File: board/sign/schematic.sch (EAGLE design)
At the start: 37 parts, among them IC1 STM32F207ZGT, IC3 LM3940, J1 DCJ0202, X2 22-23-2041

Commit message: Board REV A done
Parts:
- C24: device rcl:CPOL-USA -> rcl:CPOL-USE2-5
- JP2: device con-lstb:MA04-1 -> con-lstb:MA05-1
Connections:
- net DEBUG_TX: now also JP2.5
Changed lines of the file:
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@@
 <part name="IC3" library="LM3940" deviceset="LM3940" device=""/>
 <part name="C23" library="rcl" library_urn="urn:adsk.eagle:library:334" deviceset="C-EU" device="025-025X050" package3d_urn="urn:adsk.eagle:package:23629/2" value="0.47uF"/>
-<part name="C24" library="rcl" library_urn="urn:adsk.eagle:library:334" deviceset="CPOL-US" device="A" package3d_urn="urn:adsk.eagle:package:23418/2" value="33uF"/>
-<part name="JP2" library="con-lstb" library_urn="urn:adsk.eagle:library:162" deviceset="MA04-1" device="" package3d_urn="urn:adsk.eagle:package:8337/1"/>
+<part name="C24" library="rcl" library_urn="urn:adsk.eagle:library:334" deviceset="CPOL-US" device="E2-5" package3d_urn="urn:adsk.eagle:package:23346/2" value="33uF"/>
+<part name="JP2" library="con-lstb" library_urn="urn:adsk.eagle:library:162" deviceset="MA05-1" device="" package3d_urn="urn:adsk.eagle:package:8332/1"/>
 <part name="JP1" library="pinhead" library_urn="urn:adsk.eagle:library:325" deviceset="PINHD-2X8" device="" package3d_urn="urn:adsk.eagle:package:22481/2"/>
 <part name="GND18" library="supply1" library_urn="urn:adsk.eagle:library:371" deviceset="GND" device=""/>
@@
 <attribute name="VALUE" x="227.076" y="224.409" size="1.778" layer="96"/>
 </instance>
-<instance part="JP2" gate="1" x="307.34" y="101.6" smashed="yes" rot="R180">
+<instance part="JP2" gate="G$1" x="307.34" y="101.6" smashed="yes" rot="R180">
 <attribute name="VALUE" x="308.61" y="111.76" size="1.778" layer="96" rot="R180"/>
-<attribute name="NAME" x="308.61" y="95.758" size="1.778" layer="95" rot="R180"/>
+<attribute name="NAME" x="313.69" y="98.298" size="1.778" layer="95" rot="R180"/>
 </instance>
 <instance part="JP1" gate="A" x="299.72" y="76.2" smashed="yes">
@@
 <pinref part="GND19" gate="1" pin="GND"/>
 <wire x1="279.4" y1="91.44" x2="279.4" y2="99.06" width="0.1524" layer="91"/>
-<pinref part="JP2" gate="1" pin="4"/>
+<pinref part="JP2" gate="G$1" pin="4"/>
 <wire x1="279.4" y1="99.06" x2="299.72" y2="99.06" width="0.1524" layer="91"/>
 </segment>
@@
 </segment>
 <segment>
-<pinref part="JP2" gate="1" pin="1"/>
+<pinref part="JP2" gate="G$1" pin="1"/>
 <wire x1="299.72" y1="106.68" x2="284.48" y2="106.68" width="0.1524" layer="91"/>
 <pinref part="+3V9" gate="G$1" pin="+3V3"/>
@@
 <junction x="83.82" y="33.02"/>
 </segment>
+<segment>
+<pinref part="JP2" gate="G$1" pin="5"/>
+<wire x1="299.72" y1="96.52" x2="281.94" y2="96.52" width="0.1524" layer="91"/>
+<label x="281.94" y="96.52" size="1.778" layer="95"/>
+</segment>
 </net>
 <net name="N$4" class="0">
@@
 </segment>
 <segment>
-<pinref part="JP2" gate="1" pin="2"/>
+<pinref part="JP2" gate="G$1" pin="2"/>
 <wire x1="299.72" y1="104.14" x2="279.4" y2="104.14" width="0.1524" layer="91"/>
 <label x="279.4" y="104.14" size="1.778" layer="95"/>
@@
 </segment>
 <segment>
-<pinref part="JP2" gate="1" pin="3"/>
+<pinref part="JP2" gate="G$1" pin="3"/>
 <wire x1="299.72" y1="101.6" x2="279.4" y2="101.6" width="0.1524" layer="91"/>
 <label x="279.4" y="101.6" size="1.778" layer="95"/>
@@
 </sheet>
 </sheets>
+<errors>
+</errors>
 </schematic>
 </drawing>

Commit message: Fix SD
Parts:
- removed U$1: MICROSD, micro-sd:MICROSD
- added J2: 2908-05WB-MG, 2908-05WB-MG:2908-05WB-MG
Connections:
- net +3V3: now also J2.VDD; no longer U$1.VDD
- net GND: now also J2.VSS; no longer U$1.GND, U$1.SHIELD@1, U$1.SHIELD@2, U$1.SHIELD@3, U$1.SHIELD@4
- net MISO: now also J2.DAT0; no longer U$1.DAT0/DO
- net MOSI: now also J2.CMD; no longer U$1.CMD/DI
- net SCLK: now also J2.CLK; no longer U$1.CLK/SCLK
- net SDCS: now also J2.DAT3/CD; no longer U$1.CD/DAT3/CS
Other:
- moved on the sheet: C21
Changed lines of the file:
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@@
 <part name="R2" library="rcl" library_urn="urn:adsk.eagle:library:334" deviceset="R-US_" device="0204/7" package3d_urn="urn:adsk.eagle:package:23498/1" value="12k"/>
 <part name="GND11" library="supply1" library_urn="urn:adsk.eagle:library:371" deviceset="GND" device=""/>
-<part name="U$1" library="micro-sd" deviceset="MICROSD" device=""/>
 <part name="+3V5" library="supply1" library_urn="urn:adsk.eagle:library:371" deviceset="+3V3" device=""/>
-<part name="GND12" library="supply1" library_urn="urn:adsk.eagle:library:371" deviceset="GND" device=""/>
 <part name="C21" library="rcl" library_urn="urn:adsk.eagle:library:334" deviceset="C-EU" device="025-025X050" package3d_urn="urn:adsk.eagle:package:23629/2" value="100nF"/>
 <part name="GND13" library="supply1" library_urn="urn:adsk.eagle:library:371" deviceset="GND" device=""/>
@@
 <part name="+3V2" library="supply1" library_urn="urn:adsk.eagle:library:371" deviceset="+3V3" device=""/>
 <part name="+3V11" library="supply1" library_urn="urn:adsk.eagle:library:371" deviceset="+3V3" device=""/>
+<part name="J2" library="2908-05WB-MG" deviceset="2908-05WB-MG" device=""/>
+<part name="GND20" library="supply1" library_urn="urn:adsk.eagle:library:371" deviceset="GND" device=""/>
 </parts>
 <sheets>
@@
 <attribute name="VALUE" x="86.36" y="15.24" size="1.778" layer="96"/>
 </instance>
-<instance part="U$1" gate="G$1" x="236.22" y="88.9" smashed="yes"/>
-<instance part="+3V5" gate="G$1" x="208.28" y="114.3" smashed="yes">
-<attribute name="VALUE" x="205.74" y="109.22" size="1.778" layer="96" rot="R90"/>
-</instance>
-<instance part="GND12" gate="1" x="208.28" y="55.88" smashed="yes">
-<attribute name="VALUE" x="205.74" y="53.34" size="1.778" layer="96"/>
-</instance>
-<instance part="C21" gate="G$1" x="205.74" y="106.68" smashed="yes" rot="R270">
-<attribute name="NAME" x="206.121" y="105.156" size="1.778" layer="95" rot="R270"/>
-<attribute name="VALUE" x="201.041" y="105.156" size="1.778" layer="96" rot="R270"/>
-</instance>
-<instance part="GND13" gate="1" x="198.12" y="106.68" smashed="yes" rot="R270">
-<attribute name="VALUE" x="195.58" y="109.22" size="1.778" layer="96" rot="R270"/>
+<instance part="+3V5" gate="G$1" x="266.7" y="109.22" smashed="yes" rot="R270">
+<attribute name="VALUE" x="261.62" y="111.76" size="1.778" layer="96"/>
+</instance>
+<instance part="C21" gate="G$1" x="259.08" y="111.76" smashed="yes" rot="R180">
+<attribute name="NAME" x="257.556" y="111.379" size="1.778" layer="95" rot="R180"/>
+<attribute name="VALUE" x="257.556" y="116.459" size="1.778" layer="96" rot="R180"/>
+</instance>
+<instance part="GND13" gate="1" x="259.08" y="119.38" smashed="yes" rot="R180">
+<attribute name="VALUE" x="261.62" y="121.92" size="1.778" layer="96" rot="R180"/>
 </instance>
 <instance part="X2" gate="-1" x="162.56" y="127" smashed="yes">
@@
 <instance part="+3V11" gate="G$1" x="289.56" y="215.9" smashed="yes">
 <attribute name="VALUE" x="287.02" y="210.82" size="1.778" layer="96" rot="R90"/>
+</instance>
+<instance part="J2" gate="G$1" x="238.76" y="93.98" smashed="yes">
+<attribute name="NAME" x="228.5841" y="104.1559" size="1.271990625" layer="95"/>
+<attribute name="VALUE" x="228.5925" y="81.2706" size="1.270940625" layer="96"/>
+</instance>
+<instance part="GND20" gate="1" x="259.08" y="78.74" smashed="yes">
+<attribute name="VALUE" x="256.54" y="76.2" size="1.778" layer="96"/>
 </instance>
 </instances>
@@
 </segment>
 <segment>
-<pinref part="GND12" gate="1" pin="GND"/>
-<pinref part="U$1" gate="G$1" pin="SHIELD@4"/>
-<wire x1="208.28" y1="58.42" x2="208.28" y2="68.58" width="0.1524" layer="91"/>
-<wire x1="208.28" y1="68.58" x2="215.9" y2="68.58" width="0.1524" layer="91"/>
-<pinref part="U$1" gate="G$1" pin="SHIELD@2"/>
-<wire x1="215.9" y1="73.66" x2="208.28" y2="73.66" width="0.1524" layer="91"/>
-<wire x1="208.28" y1="73.66" x2="208.28" y2="71.12" width="0.1524" layer="91"/>
-<junction x="208.28" y="68.58"/>
-<pinref part="U$1" gate="G$1" pin="SHIELD@3"/>
-<wire x1="208.28" y1="71.12" x2="208.28" y2="68.58" width="0.1524" layer="91"/>
-<wire x1="208.28" y1="71.12" x2="215.9" y2="71.12" width="0.1524" layer="91"/>
-<junction x="208.28" y="71.12"/>
-<pinref part="U$1" gate="G$1" pin="SHIELD@1"/>
-<wire x1="215.9" y1="76.2" x2="208.28" y2="76.2" width="0.1524" layer="91"/>
-<wire x1="208.28" y1="76.2" x2="208.28" y2="73.66" width="0.1524" layer="91"/>
-<junction x="208.28" y="73.66"/>
-<pinref part="U$1" gate="G$1" pin="GND"/>
-<wire x1="215.9" y1="78.74" x2="208.28" y2="78.74" width="0.1524" layer="91"/>
-<wire x1="208.28" y1="78.74" x2="208.28" y2="76.2" width="0.1524" layer="91"/>
-<junction x="208.28" y="76.2"/>
-</segment>
-<segment>
 <pinref part="C21" gate="G$1" pin="2"/>
 <pinref part="GND13" gate="1" pin="GND"/>
@@
 <pinref part="GND2" gate="1" pin="GND"/>
 <junction x="20.32" y="119.38"/>
+</segment>
+<segment>
+<pinref part="GND20" gate="1" pin="GND"/>
+<wire x1="259.08" y1="81.28" x2="259.08" y2="86.36" width="0.1524" layer="91"/>
+<pinref part="J2" gate="G$1" pin="VSS"/>
+<wire x1="259.08" y1="86.36" x2="254" y2="86.36" width="0.1524" layer="91"/>
 </segment>
 </net>
@@
 <segment>
 <pinref part="+3V5" gate="G$1" pin="+3V3"/>
-<pinref part="U$1" gate="G$1" pin="VDD"/>
-<wire x1="208.28" y1="111.76" x2="208.28" y2="106.68" width="0.1524" layer="91"/>
-<wire x1="208.28" y1="106.68" x2="215.9" y2="106.68" width="0.1524" layer="91"/>
+<wire x1="264.16" y1="109.22" x2="259.08" y2="109.22" width="0.1524" layer="91"/>
+<wire x1="259.08" y1="109.22" x2="259.08" y2="101.6" width="0.1524" layer="91"/>
 <pinref part="C21" gate="G$1" pin="1"/>
-<junction x="208.28" y="106.68"/>
+<junction x="259.08" y="109.22"/>
+<pinref part="J2" gate="G$1" pin="VDD"/>
+<wire x1="259.08" y1="101.6" x2="254" y2="101.6" width="0.1524" layer="91"/>
 </segment>
 <segment>
@@
 <net name="SCLK" class="0">
 <segment>
-<pinref part="U$1" gate="G$1" pin="CLK/SCLK"/>
-<wire x1="215.9" y1="99.06" x2="187.96" y2="99.06" width="0.1524" layer="91"/>
-<label x="187.96" y="99.06" size="1.778" layer="95"/>
-</segment>
-<segment>
 <pinref part="IC2" gate="G$1" pin="GPIO14"/>
 <wire x1="27.94" y1="35.56" x2="17.78" y2="35.56" width="0.1524" layer="91"/>
 <label x="17.78" y="35.56" size="1.778" layer="95"/>
 </segment>
+<segment>
+<pinref part="J2" gate="G$1" pin="CLK"/>
+<wire x1="223.52" y1="86.36" x2="208.28" y2="86.36" width="0.1524" layer="91"/>
+<label x="208.28" y="86.36" size="1.778" layer="95"/>
+</segment>
 </net>
 <net name="MOSI" class="0">
-<segment>
-<pinref part="U$1" gate="G$1" pin="CMD/DI"/>
-<wire x1="215.9" y1="101.6" x2="187.96" y2="101.6" width="0.1524" layer="91"/>
-<label x="187.96" y="101.6" size="1.778" layer="95"/>
-</segment>
 <segment>
 <pinref part="IC2" gate="G$1" pin="GPIO4"/>
@@
 <label x="68.58" y="48.26" size="1.778" layer="95" rot="R90"/>
 </segment>
+<segment>
+<pinref part="J2" gate="G$1" pin="CMD"/>
+<wire x1="223.52" y1="91.44" x2="208.28" y2="91.44" width="0.1524" layer="91"/>
+<label x="208.28" y="91.44" size="1.778" layer="95"/>
+</segment>
 </net>
 <net name="MISO" class="0">
-<segment>
-<pinref part="U$1" gate="G$1" pin="DAT0/DO"/>
-<wire x1="215.9" y1="96.52" x2="187.96" y2="96.52" width="0.1524" layer="91"/>
-<label x="187.96" y="96.52" size="1.778" layer="95"/>
-</segment>
 <segment>
 <pinref part="IC2" gate="G$1" pin="GPIO12"/>
@@
 <label x="10.16" y="33.02" size="1.778" layer="95"/>
 </segment>
+<segment>
+<pinref part="J2" gate="G$1" pin="DAT0"/>
+<wire x1="223.52" y1="101.6" x2="208.28" y2="101.6" width="0.1524" layer="91"/>
+<label x="208.28" y="101.6" size="1.778" layer="95"/>
+</segment>
 </net>
 <net name="SDCS" class="0">
-<segment>
-<pinref part="U$1" gate="G$1" pin="CD/DAT3/CS"/>
-<wire x1="215.9" y1="88.9" x2="187.96" y2="88.9" width="0.1524" layer="91"/>
-<label x="187.96" y="88.9" size="1.778" layer="95"/>
-</segment>
 <segment>
 <pinref part="IC2" gate="G$1" pin="GPIO5"/>
@@
 <label x="66.04" y="48.26" size="1.778" layer="95" rot="R90"/>
 </segment>
-</net>
+<segment>
+<pinref part="J2" gate="G$1" pin="DAT3/CD"/>
+<wire x1="223.52" y1="93.98" x2="208.28" y2="93.98" width="0.1524" layer="91"/>
+<label x="208.28" y="93.98" size="1.778" layer="95"/>
+</segment>
+</net>

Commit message: Final board
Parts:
- removed J2: 2908-05WB-MG, 2908-05WB-MG:2908-05WB-MG
- added J3: DM3AT-SF-PEJM5, connector:DM3AT-SF-PEJM5
- added R5: 470, rcl:R-US_0204/7
- added S2: (no value), switch-omron:10-XX
- C19: device rcl:C-EU025-025X050 -> rcl:CPOL-USE2.5-6
- C2, C23: device rcl:C-EU025-025X050 -> rcl:C-EU050-024X044
- C4, C5: device rcl:C-EU025-025X050 -> rcl:CPOL-USE1.8-4
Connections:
- removed net N$4: IC2.GPIO0, R3.2
- new net FLASH: IC2.GPIO0, R3.2, R5.2
- new net N$1: R5.1, S2.S, S2.S1
- net +3V3: now also C19.+, J3.VCC; no longer C19.1, J2.VDD
- net GND: now also C19.-, C4.-, C5.-, J3.GND, S2.P, S2.P1; no longer C19.2, C4.1, C5.1, J2.VSS
- net MISO: now also J3.DATA0/MISO; no longer J2.DAT0
- net MOSI: now also J3.CMD/MOSI; no longer J2.CMD
- net N$2: now also C5.+; no longer C5.2
- net N$3: now also C4.+; no longer C4.2
- net SCLK: now also J3.CLK; no longer J2.CLK
- net SDCS: now also J3.DATA3-CD/CS_N; no longer J2.DAT3/CD
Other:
- moved on the sheet: C21

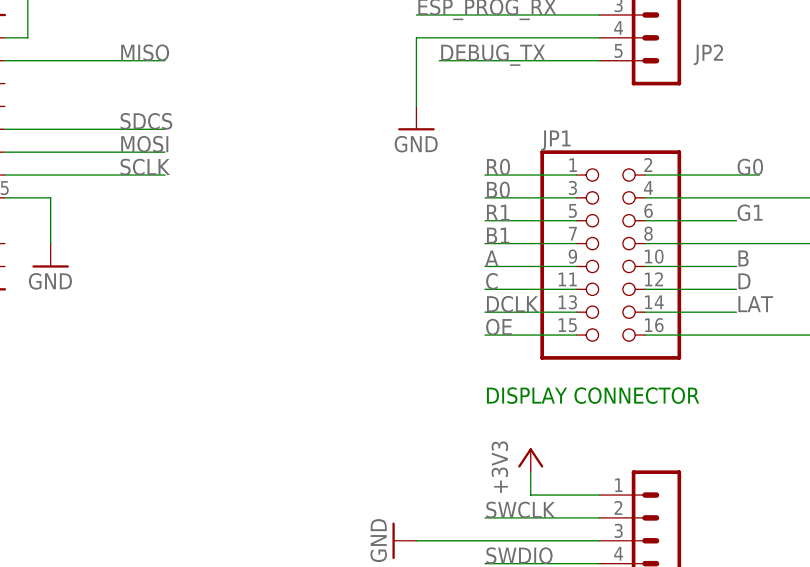
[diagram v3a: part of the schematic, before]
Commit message: Add noise-cleanup cap
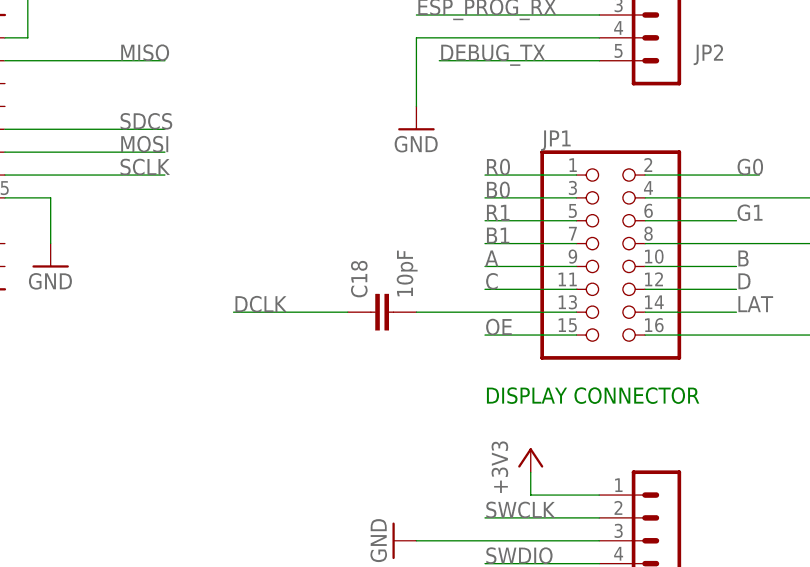
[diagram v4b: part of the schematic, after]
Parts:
- added C18: 10pF, rcl:C-EU050-024X044
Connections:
- new net N$4: C18.2, JP1.13
- net DCLK: now also C18.1; no longer JP1.13
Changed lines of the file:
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@@
 <part name="GND4" library="supply1" library_urn="urn:adsk.eagle:library:371" deviceset="GND" device=""/>
 <part name="J3" library="connector" deviceset="DM3AT-SF-PEJM5" device=""/>
+<part name="C18" library="rcl" library_urn="urn:adsk.eagle:library:334" deviceset="C-EU" device="050-024X044" package3d_urn="urn:adsk.eagle:package:23643/1" value="10pF"/>
 </parts>
 <sheets>
@@
 <attribute name="VALUE" x="205.74" y="68.58" size="1.27" layer="96"/>
 </instance>
+<instance part="C18" gate="G$1" x="274.32" y="68.58" smashed="yes" rot="R90">
+<attribute name="NAME" x="273.939" y="70.104" size="1.778" layer="95" rot="R90"/>
+<attribute name="VALUE" x="279.019" y="70.104" size="1.778" layer="96" rot="R90"/>
+</instance>
 </instances>
 <busses>
@@
 </segment>
 <segment>
-<pinref part="JP1" gate="A" pin="13"/>
-<wire x1="297.18" y1="68.58" x2="287.02" y2="68.58" width="0.1524" layer="91"/>
-<label x="287.02" y="68.58" size="1.778" layer="95"/>
+<pinref part="C18" gate="G$1" pin="1"/>
+<wire x1="271.78" y1="68.58" x2="259.08" y2="68.58" width="0.1524" layer="91"/>
+<label x="259.08" y="68.58" size="1.778" layer="95"/>
 </segment>
 </net>
@@
 </segment>
 </net>
+<net name="N$4" class="0">
+<segment>
+<pinref part="JP1" gate="A" pin="13"/>
+<pinref part="C18" gate="G$1" pin="2"/>
+<wire x1="297.18" y1="68.58" x2="279.4" y2="68.58" width="0.1524" layer="91"/>
+</segment>
+</net>

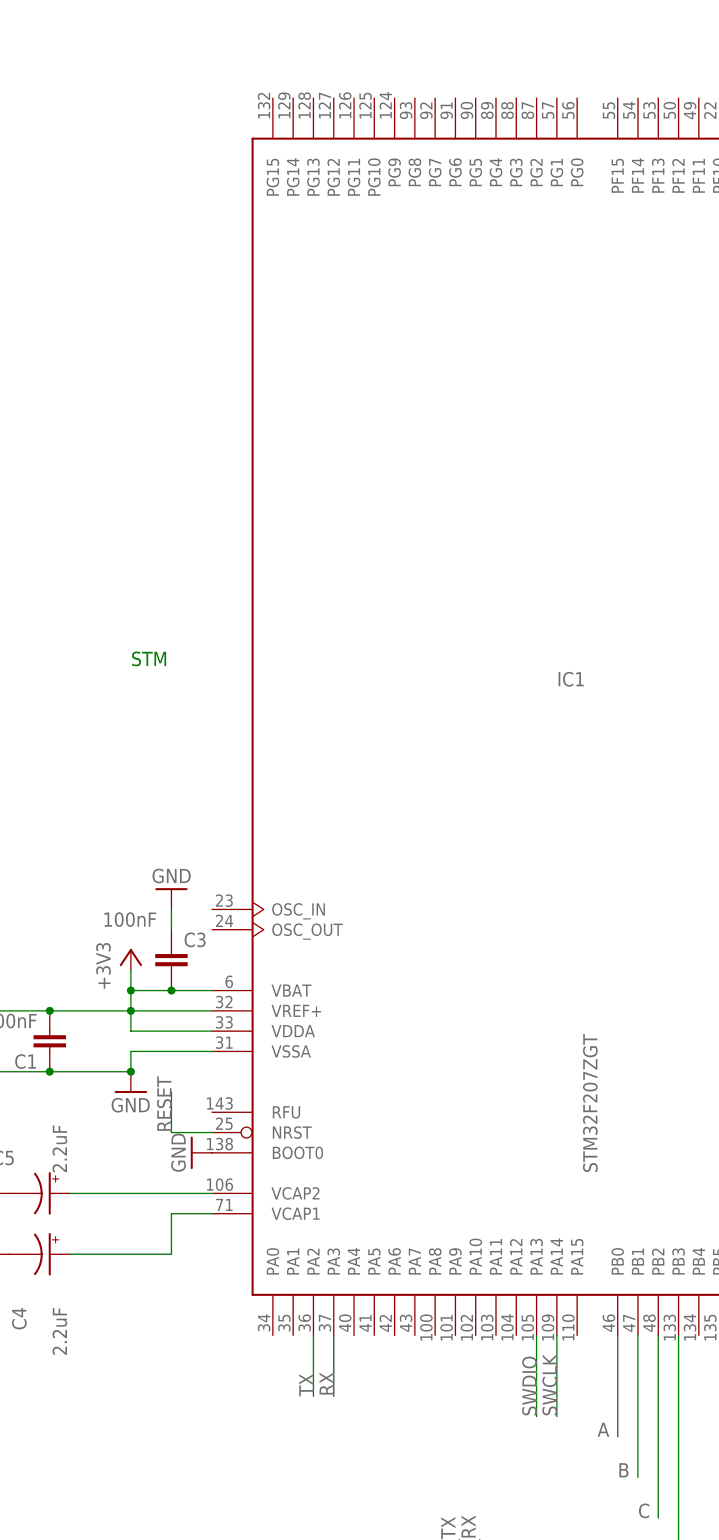
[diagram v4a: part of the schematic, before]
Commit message: Fix board again -- god damned incorrect docs
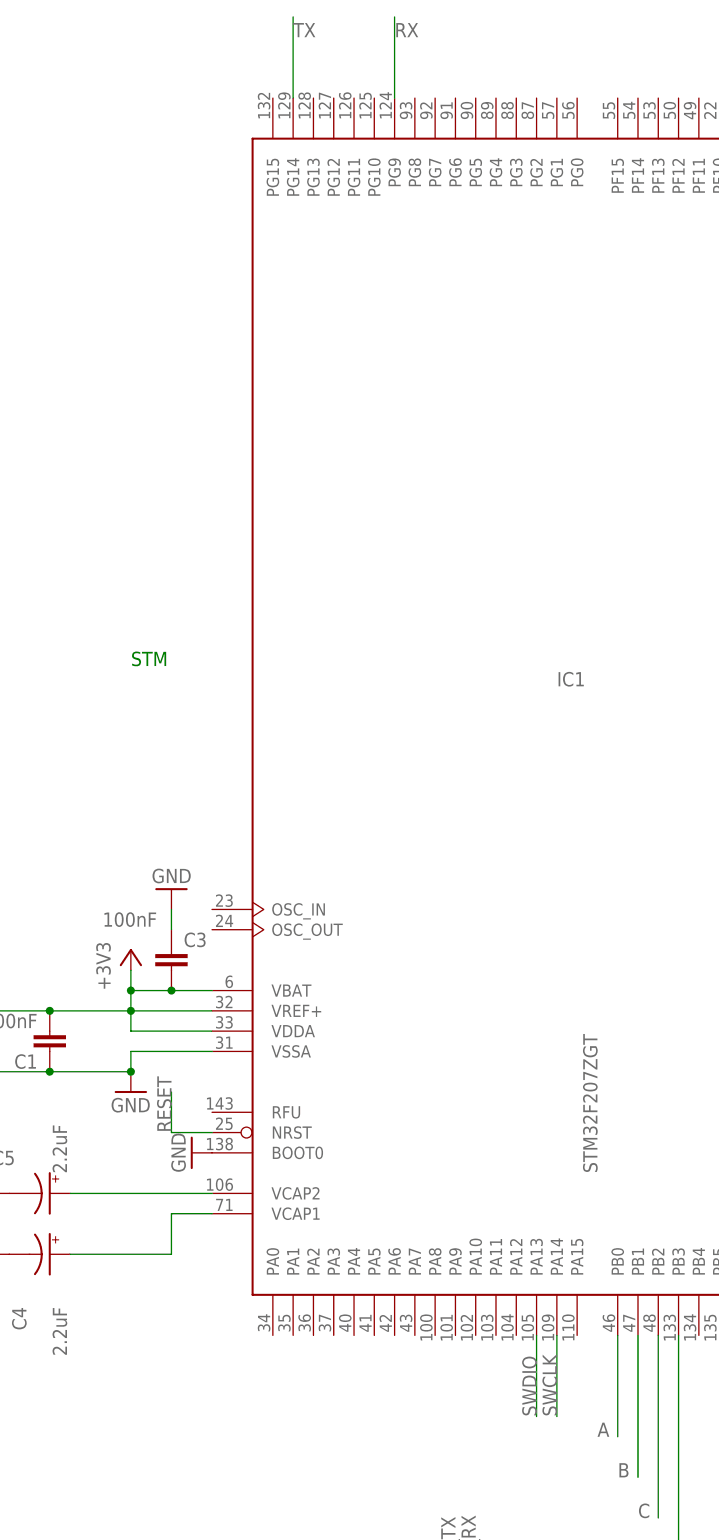
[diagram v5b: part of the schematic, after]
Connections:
- net RX: now also IC1MCU.PG9; no longer IC1MCU.PA3
- net TX: now also IC1MCU.PG14; no longer IC1MCU.PA2
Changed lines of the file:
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@@
 <net name="TX" class="0">
-<segment>
-<pinref part="IC1" gate="MCU" pin="PA2"/>
-<wire x1="43.18" y1="86.36" x2="43.18" y2="78.74" width="0.1524" layer="91"/>
-<label x="43.18" y="78.74" size="1.778" layer="95" rot="R90"/>
-</segment>
 <segment>
 <pinref part="IC2" gate="G$1" pin="GPIO13"/>
@@
 <label x="10.16" y="30.48" size="1.778" layer="95"/>
 </segment>
+<segment>
+<pinref part="IC1" gate="MCU" pin="PG14"/>
+<wire x1="40.64" y1="241.3" x2="40.64" y2="251.46" width="0.1524" layer="91"/>
+<label x="40.64" y="248.92" size="1.778" layer="95"/>
+</segment>
 </net>
 <net name="RX" class="0">
-<segment>
-<pinref part="IC1" gate="MCU" pin="PA3"/>
-<wire x1="45.72" y1="86.36" x2="45.72" y2="78.74" width="0.1524" layer="91"/>
-<label x="45.72" y="78.74" size="1.778" layer="95" rot="R90"/>
-</segment>
 <segment>
 <pinref part="IC2" gate="G$1" pin="GPIO15"/>
@@
 <junction x="88.9" y="30.48"/>
 </segment>
+<segment>
+<pinref part="IC1" gate="MCU" pin="PG9"/>
+<wire x1="53.34" y1="241.3" x2="53.34" y2="251.46" width="0.1524" layer="91"/>
+<label x="53.34" y="248.92" size="1.778" layer="95"/>
+</segment>
 </net>
